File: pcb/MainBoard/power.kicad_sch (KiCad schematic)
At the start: 50 parts

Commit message: pcb: main board - contd
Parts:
- removed C? (x3): 100n, Capacitor_SMD:C_0402_1005Metric, symbol Device:C
- removed C? (x6): 220p, Capacitor_SMD:C_0402_1005Metric, symbol Device:C
- removed C? (x2): 4.7uF, Capacitor_SMD:C_0805_2012Metric, symbol Device:C_Small
- removed J? (x4): Conn_01x01, Connector_PinHeader_2.54mm:PinHeader_1x01_P2.54mm_Vertical, symbol Connector_Generic:Conn_01x01
- removed J?: Screw_Terminal_01x02, TerminalBlock:TerminalBlock_bornier-2_P5.08mm, symbol Connector:Screw_Terminal_01x02
- removed R? (x4): 470R, Resistor_SMD:R_0402_1005Metric, symbol Device:R
- removed R? (x4): 18k, Resistor_SMD:R_0402_1005Metric, symbol Device:R
- removed R? (x2): 1k, Resistor_SMD:R_0603_1608Metric, symbol Device:R
- removed R?: 21m, Experiments:ShuntResistor, symbol Device:R
- removed R?: 100mΩ, Resistor_SMD:R_1206_3216Metric, symbol Device:R
- removed R?: 1k, Resistor_SMD:R_0402_1005Metric, symbol Device:R
- removed R?: 47k, Resistor_SMD:R_0402_1005Metric, symbol Device:R
- removed TP? (x5): TestPoint, TestPoint:TestPoint_Pad_D1.0mm, symbol Connector:TestPoint
- removed U?: XC6206PxxxMR-Regulator_Linear, Package_TO_SOT_SMD:SOT-23, symbol kicad-keyboard-parts:XC6206PxxxMR-Regulator_Linear
- removed U? (x5): LM324DT, Package_SO:SOIC-14_3.9x8.7mm_P1.27mm, symbol Amplifier_Operational:LM324
- added C? (x3): 22uF, Capacitor_SMD:C_1206_3216Metric, symbol Device:C
- added C?: 100nF, Capacitor_SMD:C_0402_1005Metric, symbol Device:C_Small
- added C?: 100u, Capacitor_Tantalum_SMD:CP_EIA-3528-15_AVX-H, symbol Device:C_Polarized
- added F?: 6V 3A 50A 6A, symbol Device:Polyfuse
- added R?: 1k, Resistor_SMD:R_0402_1005Metric, symbol Device:R_Small
- added TP? (x3): TestPoint, TestPoint:TestPoint_Pad_D1.0mm, symbol Connector:TestPoint
- added U?: INA180A1, Package_TO_SOT_SMD:SOT-23-5, symbol Amplifier_Current:INA180A1
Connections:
- net +3V3 is gone; now on net 3V3: C?.1, C?.1, U?.2 (VO)
- net Load+ is gone; now on net 5V: R?.2, R?.2, R?.2, TP?.1
- net 3V3: now also C?.1, TP?.1, U?.5 (V+)
- net 5V: now also C?.1, R?.1, U?.4 (-)
- net GND: now also C?.2, C?.2, C?.2, C?.2, C?.2, R?.2, U?.2 (GND)
- net Isense: now also U?.1
- net VBUS: now also C?.1, C?.1, C?.1, F?.2, TP?.1
- net +5V renamed 5V_FILTERED
- net 5V_FILTERED: now also F?.1, TP?.1, U?.3 (+)
- no-connect marks 3 -> 0
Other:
- note removed: "High-side current sensing circuit"
- note removed: "Low-side current sensing circuit"
- note removed: "Opamp"
- note removed: "Voltage regulator"
- note removed: "Voltage sensing"
- moved on the sheet: C?, TP?, U?

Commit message: pcb progress
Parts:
- F701: renamed from F?; footprint (none) -> Fuse:Fuse_1210_3225Metric_Pad1.42x2.65mm_HandSolder
- gave numbers to parts that had none: 19
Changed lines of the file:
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@@
 		(on_board yes)
 		(dnp no)
-		(property "Reference" "C?"
+		(property "Reference" "C703"
 			(at 196.85 42.672 0)
 			(effects
@@
 			(project "MainBoard"
 				(path "/ac576ee3-ac6f-4244-babf-9af36c7a7db3/dd417ba1-23df-493d-8bf9-742d6a12b9ca"
-					(reference "C?")
+					(reference "C703")
 					(unit 1)
 				)
@@
 		(on_board yes)
 		(dnp no)
-		(property "Reference" "U?"
+		(property "Reference" "U702"
 			(at 79.248 103.378 0)
 			(effects
@@
 			(project "MainBoard"
 				(path "/ac576ee3-ac6f-4244-babf-9af36c7a7db3/dd417ba1-23df-493d-8bf9-742d6a12b9ca"
-					(reference "U?")
+					(reference "U702")
 					(unit 1)
 				)
@@
 		(dnp no)
 		(fields_autoplaced yes)
-		(property "Reference" "#PWR043"
+		(property "Reference" "#PWR0708"
 			(at 45.72 157.48 0)
 			(effects
@@
 			(project "MainBoard"
 				(path "/ac576ee3-ac6f-4244-babf-9af36c7a7db3/dd417ba1-23df-493d-8bf9-742d6a12b9ca"
-					(reference "#PWR043")
+					(reference "#PWR0708")
 					(unit 1)
 				)
@@
 		(on_board yes)
 		(dnp no)
-		(property "Reference" "TP?"
+		(property "Reference" "TP701"
 			(at 196.088 24.638 0)
 			(effects
@@
 			(project "MainBoard"
 				(path "/ac576ee3-ac6f-4244-babf-9af36c7a7db3/dd417ba1-23df-493d-8bf9-742d6a12b9ca"
-					(reference "TP?")
+					(reference "TP701")
 					(unit 1)
 				)
@@
 		(dnp no)
 		(fields_autoplaced yes)
-		(property "Reference" "#PWR066"
+		(property "Reference" "#PWR0707"
 			(at 72.39 127 0)
 			(effects
@@
 			(project "MainBoard"
 				(path "/ac576ee3-ac6f-4244-babf-9af36c7a7db3/dd417ba1-23df-493d-8bf9-742d6a12b9ca"
-					(reference "#PWR066")
+					(reference "#PWR0707")
 					(unit 1)
 				)
@@
 		(on_board yes)
 		(dnp no)
-		(property "Reference" "TP?"
+		(property "Reference" "TP703"
 			(at 89.408 28.448 0)
 			(effects
@@
 			(project "MainBoard"
 				(path "/ac576ee3-ac6f-4244-babf-9af36c7a7db3/dd417ba1-23df-493d-8bf9-742d6a12b9ca"
-					(reference "TP?")
+					(reference "TP703")
 					(unit 1)
 				)
@@
 		(dnp no)
 		(fields_autoplaced yes)
-		(property "Reference" "R?"
+		(property "Reference" "R703"
 			(at 35.56 111.76 90)
 			(effects
@@
 			(project "MainBoard"
 				(path "/ac576ee3-ac6f-4244-babf-9af36c7a7db3/dd417ba1-23df-493d-8bf9-742d6a12b9ca"
-					(reference "R?")
+					(reference "R703")
 					(unit 1)
 				)
@@
 		(dnp no)
 		(fields_autoplaced yes)
-		(property "Reference" "R?"
+		(property "Reference" "R701"
 			(at 128.27 88.8999 0)
 			(effects
@@
 			(project "MainBoard"
 				(path "/ac576ee3-ac6f-4244-babf-9af36c7a7db3/dd417ba1-23df-493d-8bf9-742d6a12b9ca"
-					(reference "R?")
+					(reference "R701")
 					(unit 1)
 				)
@@
 		(on_board yes)
 		(dnp no)
-		(property "Reference" "TP?"
+		(property "Reference" "TP702"
 			(at 69.088 28.448 0)
 			(effects
@@
 			(project "MainBoard"
 				(path "/ac576ee3-ac6f-4244-babf-9af36c7a7db3/dd417ba1-23df-493d-8bf9-742d6a12b9ca"
-					(reference "TP?")
+					(reference "TP702")
 					(unit 1)
 				)
@@
 		(dnp no)
 		(fields_autoplaced yes)
-		(property "Reference" "C?"
+		(property "Reference" "C708"
 			(at 49.53 143.5099 0)
 			(effects
@@
 			(project "MainBoard"
 				(path "/ac576ee3-ac6f-4244-babf-9af36c7a7db3/dd417ba1-23df-493d-8bf9-742d6a12b9ca"
-					(reference "C?")
+					(reference "C708")
 					(unit 1)
 				)
@@
 		(dnp no)
 		(fields_autoplaced yes)
-		(property "Reference" "#PWR046"
+		(property "Reference" "#PWR0703"
 			(at 184.15 54.61 0)
 			(effects
@@
 			(project "MainBoard"
 				(path "/ac576ee3-ac6f-4244-babf-9af36c7a7db3/dd417ba1-23df-493d-8bf9-742d6a12b9ca"
-					(reference "#PWR046")
+					(reference "#PWR0703")
 					(unit 1)
 				)
@@
 		(on_board yes)
 		(dnp no)
-		(property "Reference" "C?"
+		(property "Reference" "C702"
 			(at 186.69 42.672 0)
 			(effects
@@
 			(project "MainBoard"
 				(path "/ac576ee3-ac6f-4244-babf-9af36c7a7db3/dd417ba1-23df-493d-8bf9-742d6a12b9ca"
-					(reference "C?")
+					(reference "C702")
 					(unit 1)
 				)
@@
 		(on_board yes)
 		(dnp no)
-		(property "Reference" "U?"
+		(property "Reference" "U701"
 			(at 174.244 26.924 0)
 			(effects
@@
 			(project "MainBoard"
 				(path "/ac576ee3-ac6f-4244-babf-9af36c7a7db3/dd417ba1-23df-493d-8bf9-742d6a12b9ca"
-					(reference "U?")
+					(reference "U701")
 					(unit 1)
 				)
@@
 		(on_board yes)
 		(dnp no)
-		(property "Reference" "C?"
+		(property "Reference" "C701"
 			(at 153.924 42.672 0)
 			(effects
@@
 			(project "MainBoard"
 				(path "/ac576ee3-ac6f-4244-babf-9af36c7a7db3/dd417ba1-23df-493d-8bf9-742d6a12b9ca"
-					(reference "C?")
+					(reference "C701")
 					(unit 1)
 				)
@@
 		(dnp no)
 		(fields_autoplaced yes)
-		(property "Reference" "C?"
+		(property "Reference" "C706"
 			(at 67.31 44.4499 0)
 			(effects
@@
 			(project "MainBoard"
 				(path "/ac576ee3-ac6f-4244-babf-9af36c7a7db3/dd417ba1-23df-493d-8bf9-742d6a12b9ca"
-					(reference "C?")
+					(reference "C706")
 					(unit 1)
 				)
@@
 		(on_board yes)
 		(dnp no)
-		(property "Reference" "TP?"
+		(property "Reference" "TP705"
 			(at 50.8 117.3479 0)
 			(effects
@@
 			(project "MainBoard"
 				(path "/ac576ee3-ac6f-4244-babf-9af36c7a7db3/dd417ba1-23df-493d-8bf9-742d6a12b9ca"
-					(reference "TP?")
+					(reference "TP705")
 					(unit 1)
 				)
@@
 		(dnp no)
 		(fields_autoplaced yes)
-		(property "Reference" "#PWR068"
+		(property "Reference" "#PWR0706"
 			(at 125.73 106.68 0)
 			(effects
@@
 			(project "MainBoard"
 				(path "/ac576ee3-ac6f-4244-babf-9af36c7a7db3/dd417ba1-23df-493d-8bf9-742d6a12b9ca"
-					(reference "#PWR068")
+					(reference "#PWR0706")
 					(unit 1)
 				)
@@
 		(dnp no)
 		(fields_autoplaced yes)
-		(property "Reference" "#PWR042"
+		(property "Reference" "#PWR0704"
 			(at 38.1 64.77 0)
 			(effects
@@
 			(project "MainBoard"
 				(path "/ac576ee3-ac6f-4244-babf-9af36c7a7db3/dd417ba1-23df-493d-8bf9-742d6a12b9ca"
-					(reference "#PWR042")
+					(reference "#PWR0704")
 					(unit 1)
 				)
@@
 		(on_board yes)
 		(dnp no)
-		(property "Reference" "C?"
+		(property "Reference" "C707"
 			(at 85.09 93.9799 0)
 			(effects
@@
 			(project "MainBoard"
 				(path "/ac576ee3-ac6f-4244-babf-9af36c7a7db3/dd417ba1-23df-493d-8bf9-742d6a12b9ca"
-					(reference "C?")
+					(reference "C707")
 					(unit 1)
 				)
@@
 		(dnp no)
 		(fields_autoplaced yes)
-		(property "Reference" "C?"
+		(property "Reference" "C705"
 			(at 54.61 44.4499 0)
 			(effects
@@
 			(project "MainBoard"
 				(path "/ac576ee3-ac6f-4244-babf-9af36c7a7db3/dd417ba1-23df-493d-8bf9-742d6a12b9ca"
-					(reference "C?")
+					(reference "C705")
 					(unit 1)
 				)
@@
 		(dnp no)
 		(fields_autoplaced yes)
-		(property "Reference" "#PWR044"
+		(property "Reference" "#PWR0701"
 			(at 161.29 54.61 0)
 			(effects
@@
 			(project "MainBoard"
 				(path "/ac576ee3-ac6f-4244-babf-9af36c7a7db3/dd417ba1-23df-493d-8bf9-742d6a12b9ca"
-					(reference "#PWR044")
+					(reference "#PWR0701")
 					(unit 1)
 				)
@@
 		(dnp no)
 		(fields_autoplaced yes)
-		(property "Reference" "#PWR067"
+		(property "Reference" "#PWR0705"
 			(at 83.82 106.68 0)
 			(effects
@@
 			(project "MainBoard"
 				(path "/ac576ee3-ac6f-4244-babf-9af36c7a7db3/dd417ba1-23df-493d-8bf9-742d6a12b9ca"
-					(reference "#PWR067")
+					(reference "#PWR0705")
 					(unit 1)
 				)
@@
 		(on_board yes)
 		(dnp no)
-		(property "Reference" "F?"
+		(property "Reference" "F701"
 			(at 77.47 30.226 90)
 			(effects
@@
 			)
 		)
-		(property "Footprint" ""
+		(property "Footprint" "Fuse:Fuse_1210_3225Metric_Pad1.42x2.65mm_HandSolder"
 			(at 72.39 38.1 0)
 			(effects
@@
 			(project "MainBoard"
 				(path "/ac576ee3-ac6f-4244-babf-9af36c7a7db3/dd417ba1-23df-493d-8bf9-742d6a12b9ca"
-					(reference "F?")
+					(reference "F701")
 					(unit 1)
 				)
@@
 		(on_board yes)
 		(dnp no)
-		(property "Reference" "#PWR045"
+		(property "Reference" "#PWR0702"
 			(at 173.99 54.61 0)
 			(effects
@@
 			(project "MainBoard"
 				(path "/ac576ee3-ac6f-4244-babf-9af36c7a7db3/dd417ba1-23df-493d-8bf9-742d6a12b9ca"
-					(reference "#PWR045")
+					(reference "#PWR0702")
 					(unit 1)
 				)
@@
 		(dnp no)
 		(fields_autoplaced yes)
-		(property "Reference" "R?"
+		(property "Reference" "R702"
 			(at 31.75 111.76 90)
 			(effects
@@
 			(project "MainBoard"
 				(path "/ac576ee3-ac6f-4244-babf-9af36c7a7db3/dd417ba1-23df-493d-8bf9-742d6a12b9ca"
-					(reference "R?")
+					(reference "R702")
 					(unit 1)
 				)
@@
 		(dnp no)
 		(fields_autoplaced yes)
-		(property "Reference" "C?"
+		(property "Reference" "C704"
 			(at 41.91 43.5609 0)
 			(effects
@@
 			(project "MainBoard"
 				(path "/ac576ee3-ac6f-4244-babf-9af36c7a7db3/dd417ba1-23df-493d-8bf9-742d6a12b9ca"
-					(reference "C?")
+					(reference "C704")
 					(unit 1)
 				)
@@
 		(dnp no)
 		(fields_autoplaced yes)
-		(property "Reference" "R?"
+		(property "Reference" "R704"
 			(at 39.37 111.76 90)
 			(effects
@@
 			(project "MainBoard"
 				(path "/ac576ee3-ac6f-4244-babf-9af36c7a7db3/dd417ba1-23df-493d-8bf9-742d6a12b9ca"
-					(reference "R?")
+					(reference "R704")
 					(unit 1)
 				)
@@
 		(on_board yes)
 		(dnp no)
-		(property "Reference" "TP?"
+		(property "Reference" "TP704"
 			(at 50.8 97.0279 0)
 			(effects
@@
 			(project "MainBoard"
 				(path "/ac576ee3-ac6f-4244-babf-9af36c7a7db3/dd417ba1-23df-493d-8bf9-742d6a12b9ca"
-					(reference "TP?")
-					(unit 1)
-				)
+					(reference "TP704")
+					(unit 1)
+				)

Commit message: dump pcb
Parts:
- removed C703: 4.7uF, Capacitor_SMD:C_0805_2012Metric, symbol Device:C_Small
- removed C705: 22uF, Capacitor_SMD:C_1206_3216Metric, symbol Device:C
- removed U701: XC6206PxxxMR-Regulator_Linear, Package_TO_SOT_SMD:SOT-23, symbol kicad-keyboard-parts:XC6206PxxxMR-Regulator_Linear
- added C703: 22u, Capacitor_SMD:C_0805_2012Metric, symbol Device:C
- added C705: 100u, Capacitor_SMD:CP_Elec_6.3x7.7, symbol Device:C_Polarized
- added C709, C710, C712: 4.7uF, Capacitor_SMD:C_0805_2012Metric, symbol Device:C_Small
- added C711: 4.7uF, Capacitor_SMD:C_0603_1608Metric, symbol Device:C_Small
- added C713: 100u, Capacitor_SMD:C_1206_3216Metric, symbol Device:C
- added C714: 100pF, Capacitor_SMD:C_0402_1005Metric, symbol Device:C_Small
- added JP701: SolderJumper_3_Open, led-matrix:SolderJumper-3_Open_RoundedPad_Smol, symbol Jumper:SolderJumper_3_Open
- added R705: 1k5, Resistor_SMD:R_0402_1005Metric, symbol Device:R_Small
- added R706: 470R, Resistor_SMD:R_0402_1005Metric, symbol Device:R
- added R707: 1k, Resistor_SMD:R_0402_1005Metric, symbol Device:R_Small
- added R708: 1k8, Resistor_SMD:R_0402_1005Metric, symbol Device:R_Small
- added R709: 150R, Resistor_SMD:R_0402_1005Metric, symbol Device:R_Small
- added TP706, TP707: TestPoint, TestPoint:TestPoint_Pad_D1.0mm, symbol Connector:TestPoint
- added U701: AMS1117-3.3, Package_TO_SOT_SMD:SOT-223-3_TabPin2, symbol Regulator_Linear:AMS1117-3.3
- added U703: XC6206PxxxMR-Regulator_Linear, Package_TO_SOT_SMD:SOT-23, symbol kicad-keyboard-parts:XC6206PxxxMR-Regulator_Linear
- added U704: CJ431, Package_TO_SOT_SMD:SOT-23, symbol Reference_Voltage:TL431DBZ
- C704: now not fitted; now left out of the parts list
- C706, C708: value 22uF -> 22u; footprint Capacitor_SMD:C_1206_3216Metric -> Capacitor_SMD:C_0805_2012Metric; LCSC C12891 -> C45783
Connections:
- net 3V3: now also C703.1, C713.1, U701.2 (VO)
- net 5V: now also C701.1, C709.1, C711.1, C714.2, R706.2, U701.3 (VI), U703.3 (VI); no longer C708.1
- net 5V_FILTERED: now also C714.1; no longer C701.1
- net GND: now also C703.2, C705.2, C709.2, C710.2, C711.2, C712.2, C713.2, R705.2, R709.2, U701.1 (GND), U703.1 (GND), U704.3 (A); no longer R701.2
- net VBUS: now also C708.1, C705.1
- net Vref: now also JP701.2 (C)
- new net: R708.2, R709.1
- new net 5V_sense: R701.2, R705.1
- new net VREF_REF: R707.2, R708.1, U704.2 (REF)
- new net VREF_REG: C710.1, JP701.3 (B), TP706.1, U703.2 (VO)
- new net VREF_SHUNT: C712.1, JP701.1 (A), R706.1, R707.1, TP707.1, U704.1 (K)
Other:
- note added: "5.5V max => 3.3"
- note added: "how to do this? I don't know! let's try a few ways lol"

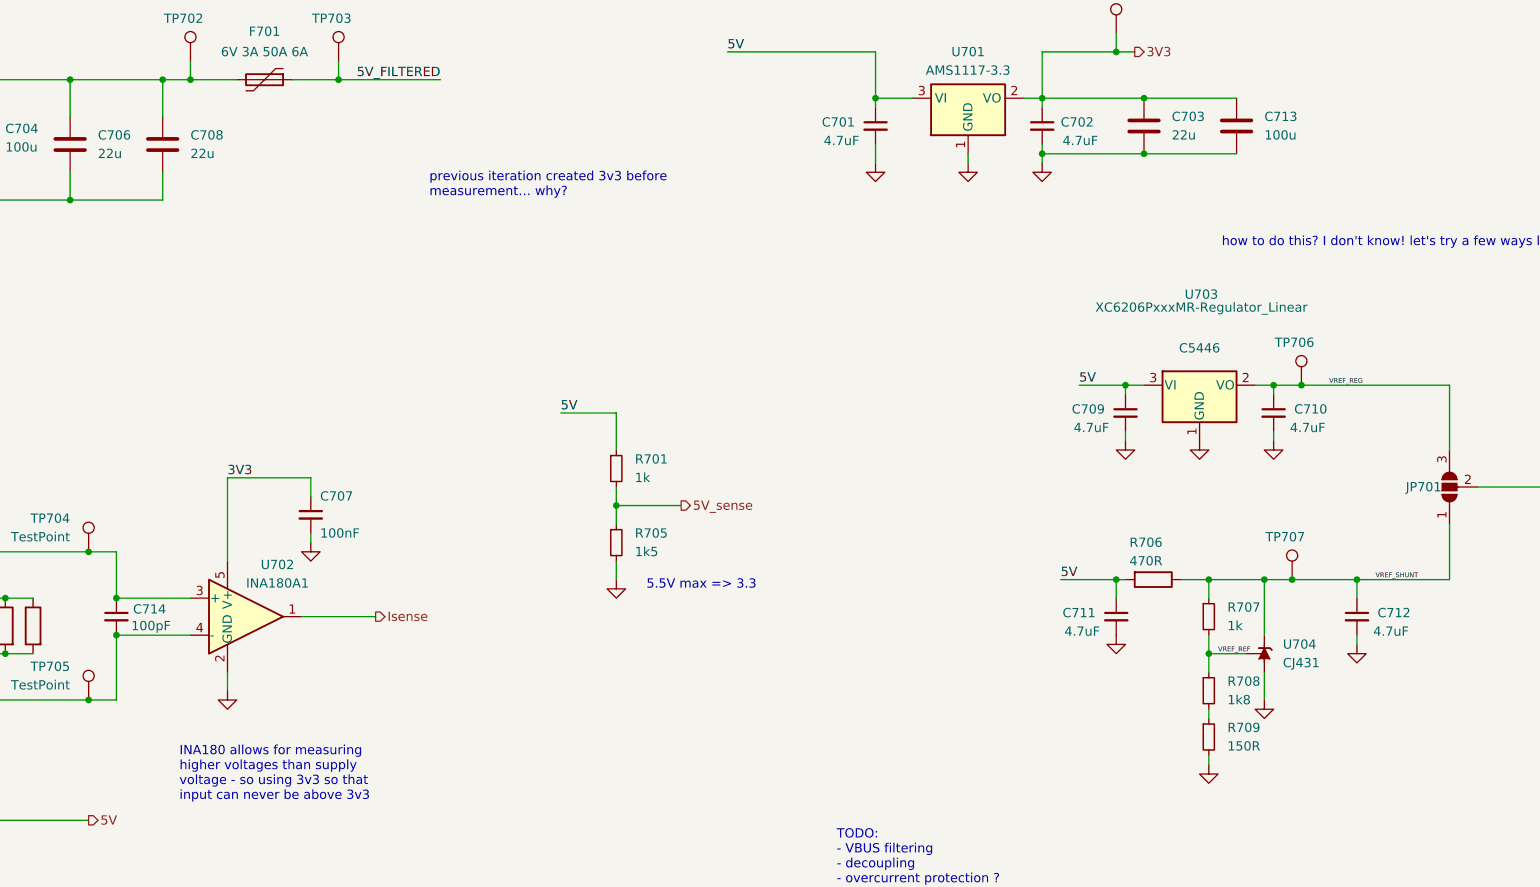
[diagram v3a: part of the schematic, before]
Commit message: MainBoard: fixes, simplify, BOM optimize, DRC fixes, ERC fixes
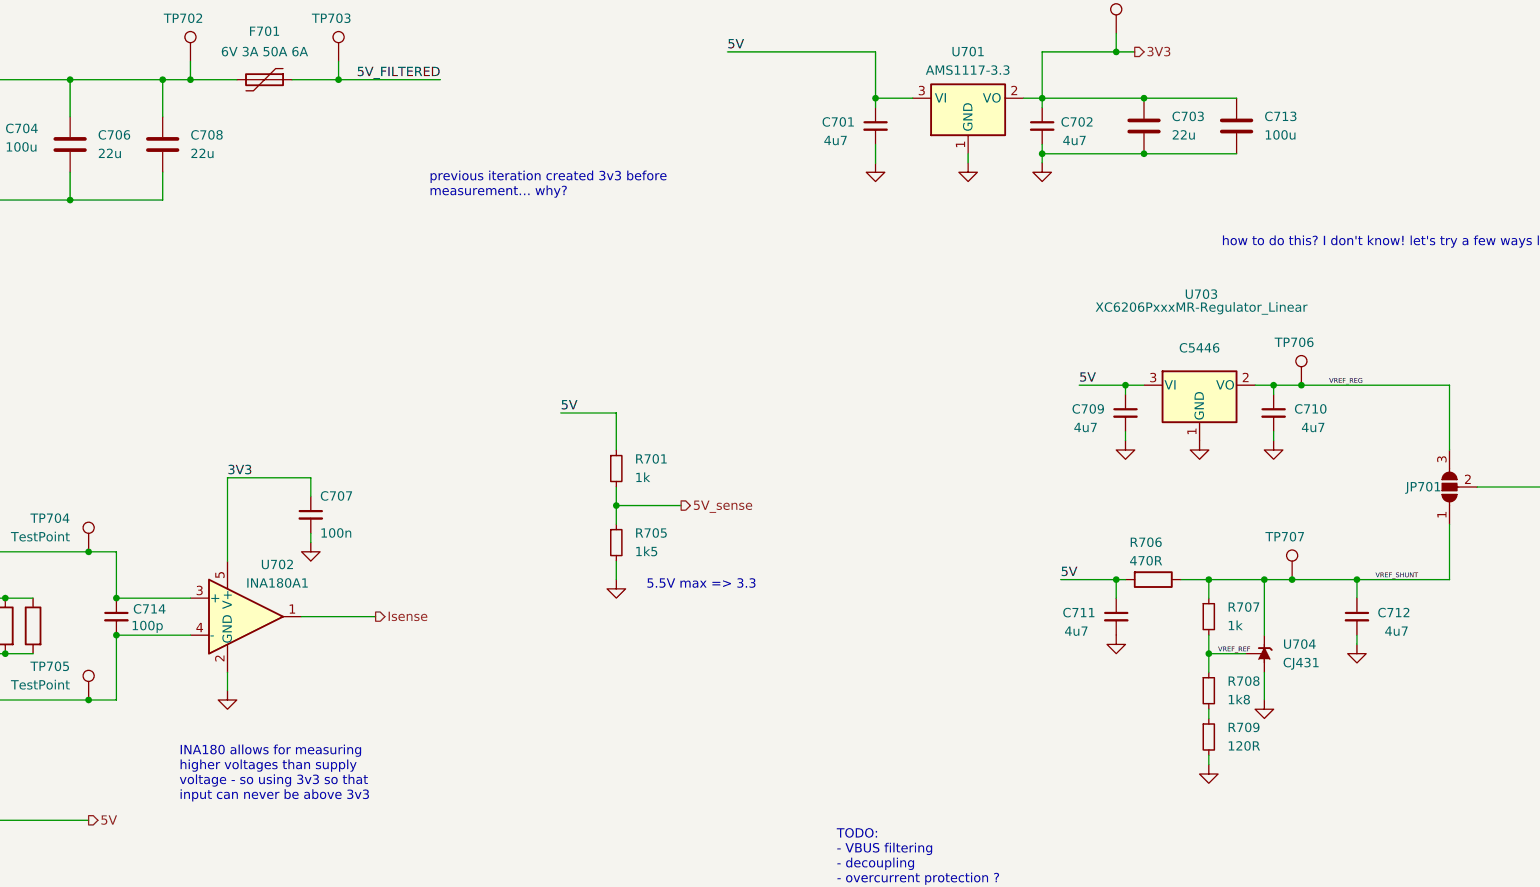
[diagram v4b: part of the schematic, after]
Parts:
- C701, C702, C709, C710, C712: value 4.7uF -> 4u7
- C707: value 100nF -> 100n
- C711: value 4.7uF -> 4u7; footprint Capacitor_SMD:C_0603_1608Metric -> Capacitor_SMD:C_0805_2012Metric; LCSC C19666 -> C1779
- C714: value 100pF -> 100p
- JP701, U702: now left out of the parts list
- R706: footprint Resistor_SMD:R_0402_1005Metric -> Resistor_SMD:R_0603_1608Metric; LCSC C25117 -> C23179
- R708: footprint Resistor_SMD:R_0402_1005Metric -> Resistor_SMD:R_0603_1608Metric; LCSC C453576 -> C4177
- R709: value 150R -> 120R; LCSC C25082 -> C25079
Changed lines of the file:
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@@
 			)
 		)
-		(property "Value" "4.7uF"
+		(property "Value" "4u7"
 			(at 234.442 112.522 0)
 			(effects
@@
 			)
 		)
-		(property "Footprint" "Resistor_SMD:R_0402_1005Metric"
+		(property "Footprint" "Resistor_SMD:R_0603_1608Metric"
 			(at 199.39 103.632 90)
 			(effects
@@
 			)
 		)
-		(property "LCSC" "C25117"
+		(property "LCSC" "C23179"
 			(at 199.39 105.41 90)
 			(effects
@@
 		(unit 1)
 		(exclude_from_sim no)
-		(in_bom yes)
+		(in_bom no)
 		(on_board yes)
 		(dnp no)
@@
 			)
 		)
-		(property "Value" "100pF"
+		(property "Value" "100p"
 			(at 59.182 111.76 0)
 			(effects
@@
 		(unit 1)
 		(exclude_from_sim no)
-		(in_bom yes)
+		(in_bom no)
 		(on_board yes)
 		(dnp no)
@@
 			)
 		)
-		(property "Value" "150R"
+		(property "Value" "120R"
 			(at 209.55 128.2699 0)
 			(effects
@@
 			)
 		)
-		(property "LCSC" "C25082"
+		(property "LCSC" "C25079"
 			(at 207.01 127 0)
 			(effects
@@
 			)
 		)
-		(property "Value" "4.7uF"
+		(property "Value" "4u7"
 			(at 186.944 45.212 0)
 			(effects
@@
 			)
 		)
-		(property "Value" "4.7uF"
+		(property "Value" "4u7"
 			(at 154.178 45.212 0)
 			(effects
@@
 			)
 		)
-		(property "Value" "4.7uF"
+		(property "Value" "4u7"
 			(at 188.468 84.582 0)
 			(effects
@@
 			)
 		)
-		(property "Value" "4.7uF"
+		(property "Value" "4u7"
 			(at 187.198 112.522 0)
 			(effects
@@
 			)
 		)
-		(property "Footprint" "Capacitor_SMD:C_0603_1608Metric"
+		(property "Footprint" "Capacitor_SMD:C_0805_2012Metric"
 			(at 194.31 110.49 0)
 			(effects
@@
 			)
 		)
-		(property "LCSC" "C19666"
+		(property "LCSC" "C1779"
 			(at 194.31 110.49 0)
 			(effects
@@
 			)
 		)
-		(property "Value" "100nF"
+		(property "Value" "100n"
 			(at 85.09 99.0599 0)
 			(effects
@@
 			)
 		)
-		(property "Value" "4.7uF"
+		(property "Value" "4u7"
 			(at 223.012 84.582 0)
 			(effects
@@
 			)
 		)
-		(property "Footprint" "Resistor_SMD:R_0402_1005Metric"
+		(property "Footprint" "Resistor_SMD:R_0603_1608Metric"
 			(at 207.01 120.65 0)
 			(effects
@@
 			)
 		)
-		(property "LCSC" "C453576"
+		(property "LCSC" "C4177"
 			(at 207.01 120.65 0)
 			(effects
